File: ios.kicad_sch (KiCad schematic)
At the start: 9 parts, among them SW1 SW_1301_9305_THT, SW2 SW_1301_9305_THT, SW3 SW_1301_9305_THT, SW4 SW_1301_9305_THT

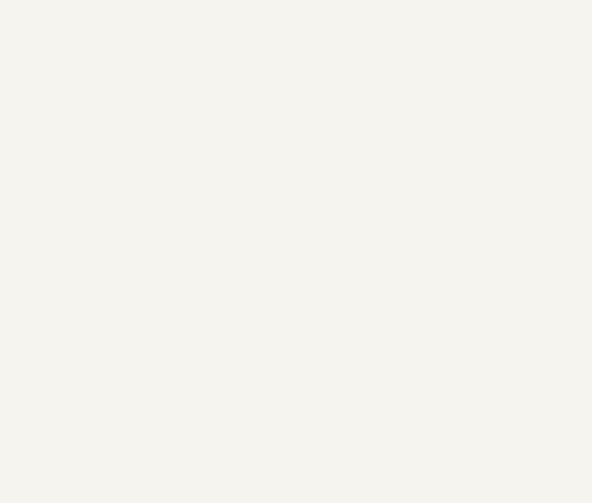
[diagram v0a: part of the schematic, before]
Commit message: [#94684] Add ports to subsheets
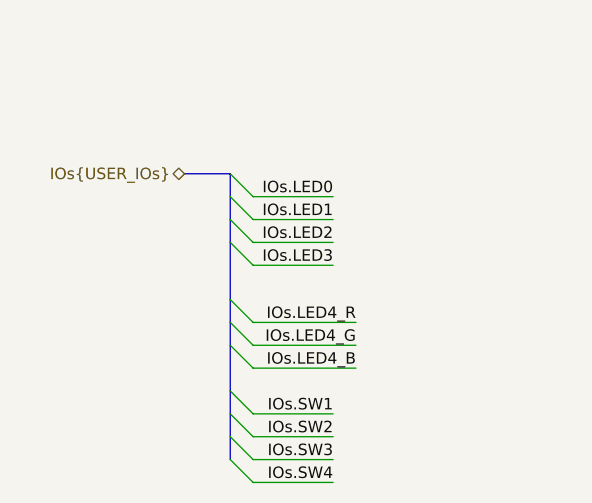
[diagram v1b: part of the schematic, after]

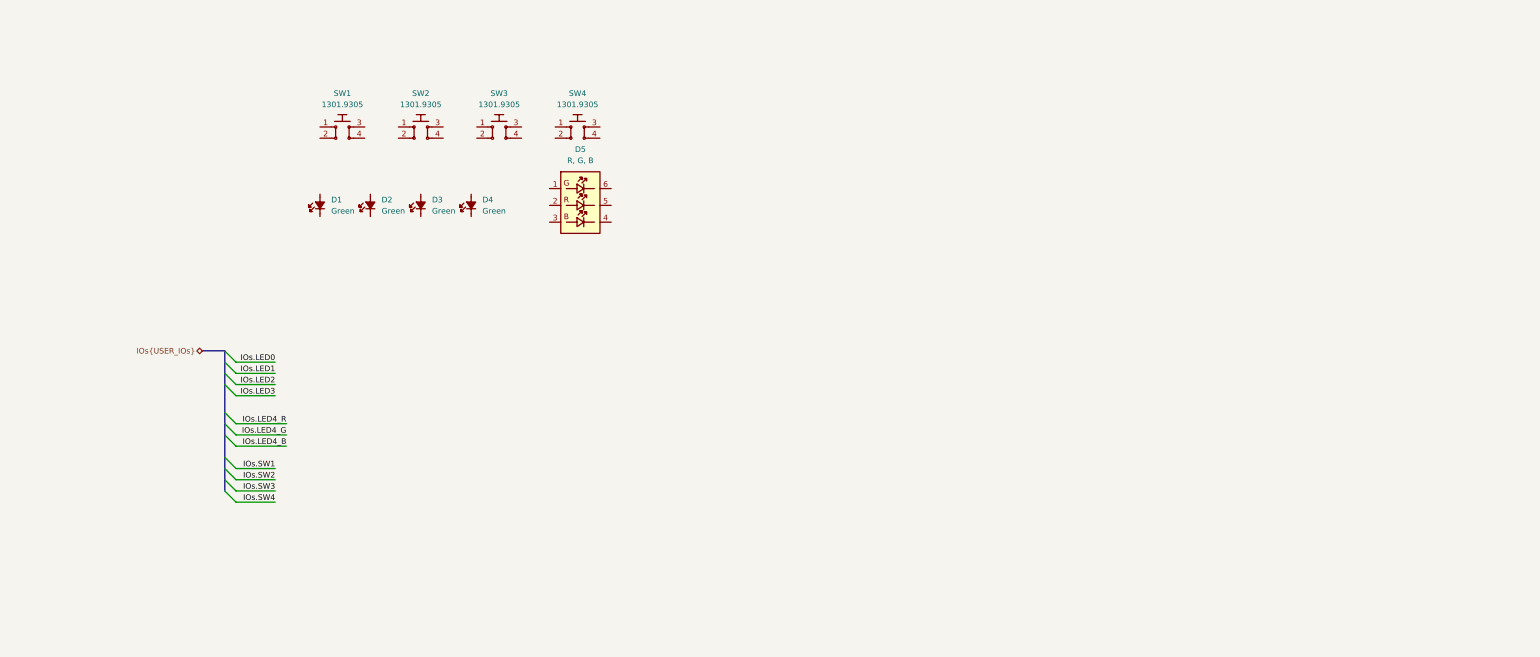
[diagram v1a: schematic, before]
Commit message: [#94883] LED and pushbutton schematic
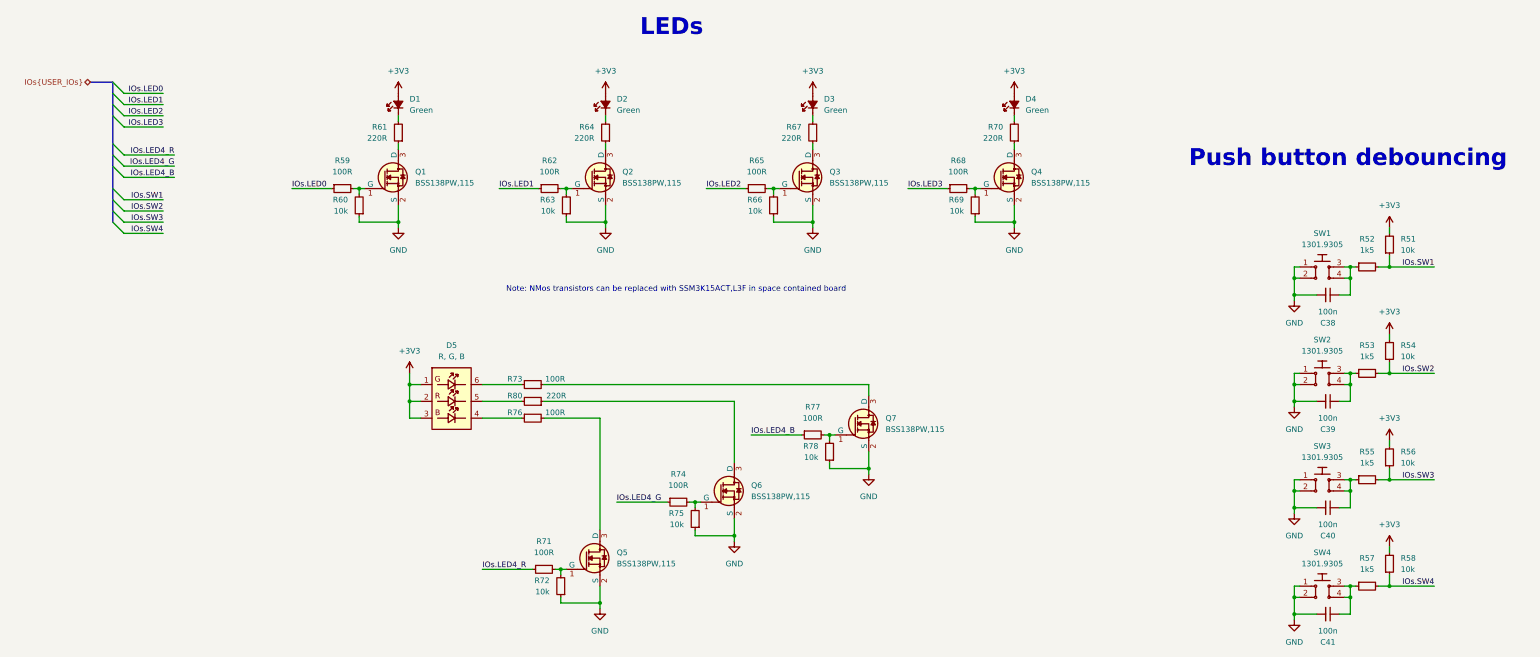
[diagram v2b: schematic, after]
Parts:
- added C38, C39, C40, C41: C_100n_0402, antmicro-footprints:C_0402_1005Metric, symbol antmicroCapacitors0402:C_100n_0402
- added Q1, Q2, Q3, Q4, Q5, Q6, Q7: BSS138PW,115, antmicro-footprints:SC70-3, symbol antmicroTransistorsFETsMOSFETsSingle:BSS138PW,115
- added R51, R54, R56, R58, R60, R63, R66, R69, R72, R75, R78: R_10k_0402, antmicro-footprints:R_0402_1005Metric, symbol antmicroResistors0402:R_10k_0402
- added R52, R53, R55, R57: R_1k5_0402, antmicro-footprints:R_0402_1005Metric, symbol antmicroResistors0402:R_1k5_0402
- added R59, R62, R65, R68, R71, R73, R74, R76, R77: R_100R_0402, antmicro-footprints:R_0402_1005Metric, symbol antmicroResistors0402:R_100R_0402
- added R61, R64, R67, R70, R80: R_220R_0402, antmicro-footprints:R_0402_1005Metric, symbol antmicroResistors0402:R_220R_0402
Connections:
- net IOs.LED0: now also R59.1
- net IOs.LED1: now also R62.1
- net IOs.LED2: now also R65.1
- net IOs.LED3: now also R68.1
- net IOs.LED4_B: now also R77.1
- net IOs.LED4_G: now also R74.1
- net IOs.LED4_R: now also R71.1
- net IOs.SW1: now also R51.1, R52.2
- net IOs.SW2: now also R53.2, R54.1
- net IOs.SW3: now also R55.2, R56.1
- net IOs.SW4: now also R57.2, R58.1
- net GND: now reaches SW4.1
- net GND: now also SW1.1, SW1.2, SW2.1, SW2.2, SW3.1, SW3.2, SW4.2, C38.2, C39.2, C40.2, C41.2, Q1.2 (S), Q2.2 (S), Q3.2 (S), Q4.2 (S), Q5.2 (S), Q6.2 (S), Q7.2 (S), R60.1, R63.1, R66.1, R69.1, R72.1, R75.1, R78.1
- net at SW4.3: now also SW4.4, C41.1, R57.1
- net at D1.1 (C): now also R61.2
- net +3V3: now reaches D1.2 (A)
- net +3V3: now also D2.2 (A), D3.2 (A), D4.2 (A), D5.1 (A_{G}), D5.2 (A_{R}), D5.3 (A_{B}), R51.2, R54.2, R56.2, R58.2
- net at SW3.3: now also SW3.4, C40.1, R55.1
- net at D3.1 (C): now also R67.2
- net at D2.1 (C): now also R64.2
- net at SW2.3: now also SW2.4, C39.1, R53.1
- net at D5.4 (C_{B}): now also R76.1
- net at D5.5 (C_{R}): now also R80.2
- net at D5.6 (C_{G}): now also R73.1
- net at SW1.3: now also SW1.4, C38.1, R52.1
- net at D4.1 (C): now also R70.2
- new net: Q4.1 (G), R68.2, R69.2
- new net: Q5.1 (G), R71.2, R72.2
- new net: Q4.3 (D), R70.1
- new net: Q2.1 (G), R62.2, R63.2
- new net: Q2.3 (D), R64.1
- new net: Q7.1 (G), R77.2, R78.2
- new net: Q6.1 (G), R74.2, R75.2
- new net: Q6.3 (D), R80.1
- new net: Q3.1 (G), R65.2, R66.2
- new net: Q7.3 (D), R73.2
- new net: Q1.1 (G), R59.2, R60.2
- new net: Q5.3 (D), R76.2
- new net: Q3.3 (D), R67.1
- new net: Q1.3 (D), R61.1
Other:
- note added: "LEDs"
- note added: "Note: NMos transistors can be replaced with SSM3K15ACT,L3F in space contained board"
- note added: "Push button debouncing"
- moved on the sheet: D1, D2, D3, D4, D5, SW1

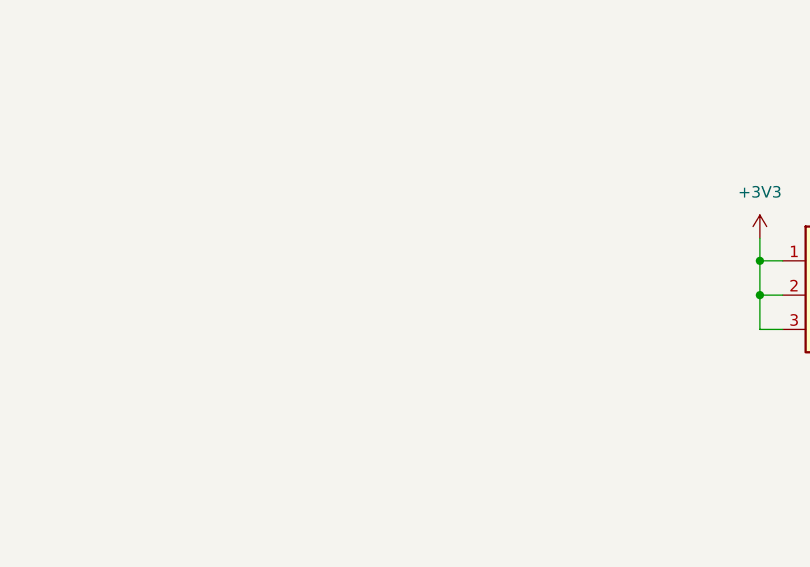
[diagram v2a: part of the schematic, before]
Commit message: [#95036] Add schematic markings
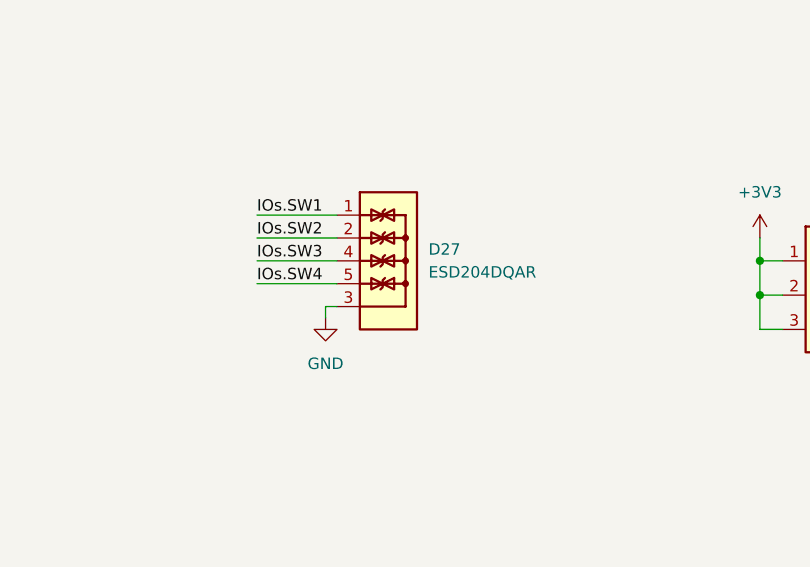
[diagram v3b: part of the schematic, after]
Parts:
- added D27: ESD204DQAR, antmicro-footprints:USON-10_2.5x1mm_P0.5mm, symbol antmicroTVSDiodes:ESD204DQAR
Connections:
- net GND: now also D27.3, D27.8
- net IOs.SW1: now also D27.1, D27.10
- net IOs.SW2: now also D27.2, D27.9
- net IOs.SW3: now also D27.4, D27.7
- net IOs.SW4: now also D27.5, D27.6

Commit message: [#95398] Cleanup
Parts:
- removed SW1, SW2, SW3, SW4: SW_1301_9305_THT, antmicro-footprints:SW_1301_9305_THT, symbol antmicroPushbuttonSwitches:SW_1301_9305_THT
- added C35, C36: C_100n_0402, antmicro-footprints:C_0402_1005Metric, symbol antmicroCapacitors0402:C_100n_0402
- added POT1, POT2: RK09K1110A2S, antmicro-footprints:Trimpot_THT_RK09K1110A2S, symbol antmicroTrimmerPotentiometers:RK09K1110A2S
- added SW1, SW2, SW3, SW4: SW_SKRPABE010, antmicro-footprints:SW_PTS810SJM250SMTRLFS_SMD, symbol antmicroPushbuttonSwitches:SW_SKRPABE010
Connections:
- net +3V3: now also POT1.1, POT2.1
- net GND: now also C35.1, C36.1, POT1.3, POT1.MH, POT2.3, POT2.MH, SW1.1, SW1.2, SW2.1, SW2.2, SW3.1, SW3.2, SW4.1, SW4.2
- net at C39.1, R53.1: now also SW2.3, SW2.4
- net at C38.1, R52.1: now also SW1.3, SW1.4
- net at C41.1, R57.1: now also SW4.3, SW4.4
- net at C40.1, R55.1: now also SW3.3, SW3.4
- new net POT1_Analog: C35.2, POT1.2
- new net POT2_Analog: C36.2, POT2.2
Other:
- moved on the sheet: C38, C39, C40, C41, D1, D2, D27, D3, D4, D5, Q1, Q2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

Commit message: [#95398] Schematic cleanup
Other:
- note added: "Potentiometers"
- note removed: "Note: NMos transistors can be replaced with SSM3K15ACT,L3F in space contained board"
- moved on the sheet: C35, C36, POT1, POT2

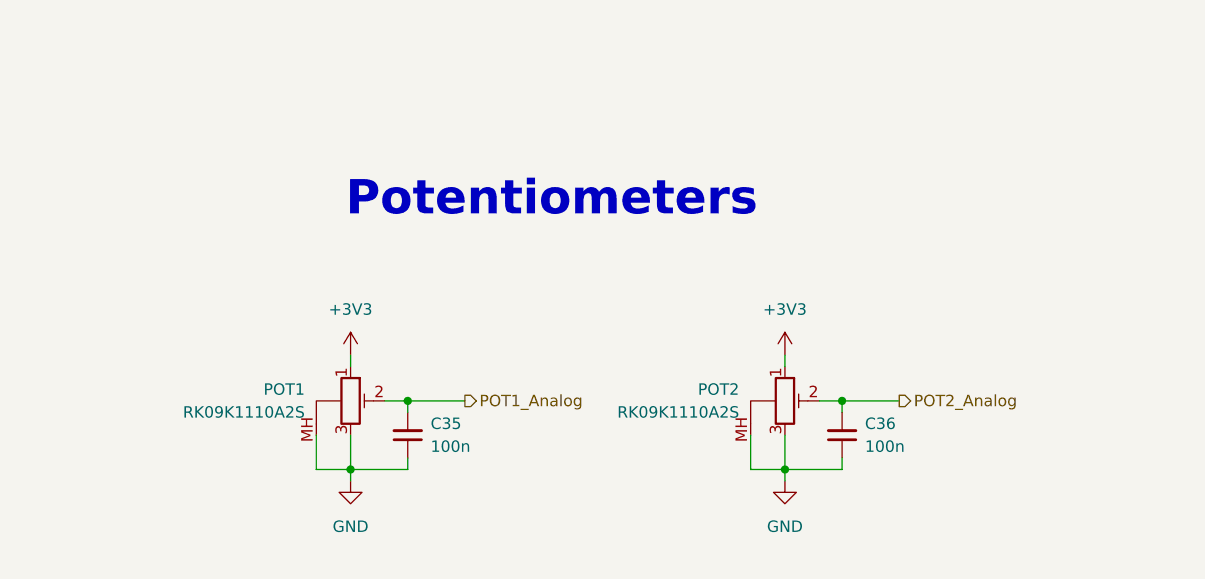
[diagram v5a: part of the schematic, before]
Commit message: [#95398] Mock main components, add BGA MCU
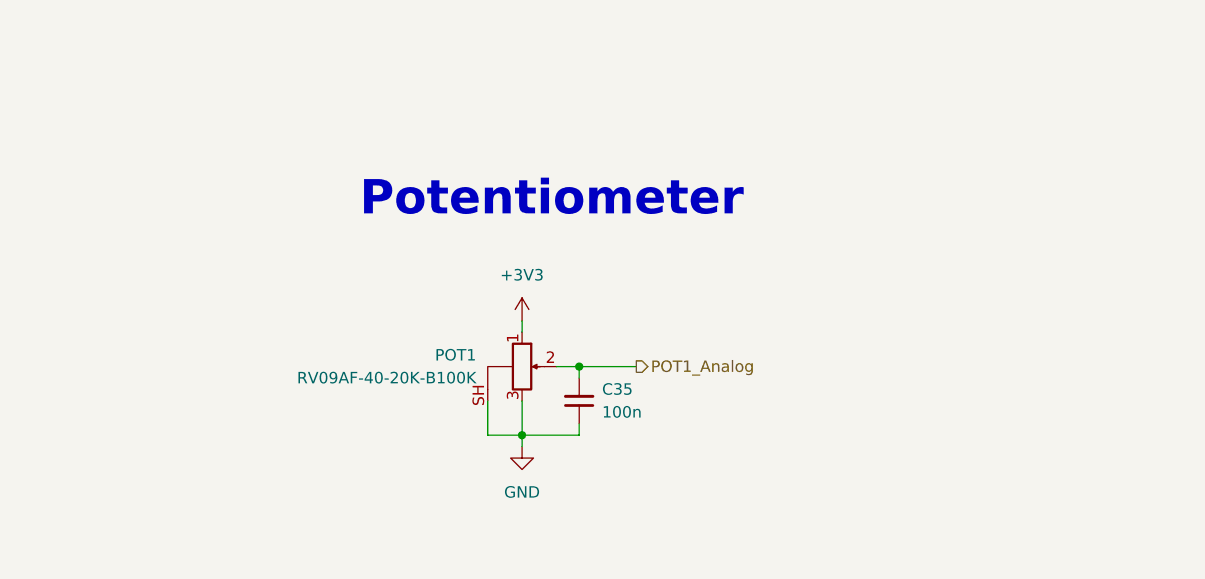
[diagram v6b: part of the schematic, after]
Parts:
- removed C36: C_100n_0402, antmicro-footprints:C_0402_1005Metric, symbol antmicroCapacitors0402:C_100n_0402
- removed POT1, POT2: RK09K1110A2S, antmicro-footprints:Trimpot_THT_RK09K1110A2S, symbol antmicroTrimmerPotentiometers:RK09K1110A2S
- added POT1: POT_100k_RV09AF-40-20K-B100K, antmicro-footprints:POT_RV09AF-40, symbol antmicroRotaryPotentiometersRheostats:POT_100k_RV09AF-40-20K-B100K
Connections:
- net +3V3: now also POT1.1
- net GND: now also POT1.3, POT1.SH
- net POT1_Analog: now also POT1.2
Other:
- note added: "Potentiometer"
- note removed: "Potentiometers"
- moved on the sheet: C35

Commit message: [#95398] Add markings for ETH strap resistors
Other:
- title: renode-reference-platform -> STM32H7 Renode Reference Platform
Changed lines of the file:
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@@
 	(paper "A3")
 	(title_block
-		(title "renode-reference-platform")
+		(title "STM32H7 Renode Reference Platform")
 		(date "07.04.2026")
 		(rev "1.0.0")

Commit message: [#95451] Finalizing final placement
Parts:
- removed Q1, Q2, Q3, Q5, Q6, Q7: BSS138PW,115, antmicro-footprints:SC70-3, symbol antmicroTransistorsFETsMOSFETsSingle:BSS138PW,115
- removed R59, R62, R65, R71, R74, R77: R_100R_0402, antmicro-footprints:R_0402_1005Metric, symbol antmicroResistors0402:R_100R_0402
- removed R60, R63, R66, R72, R75, R78: R_10k_0402, antmicro-footprints:R_0402_1005Metric, symbol antmicroResistors0402:R_10k_0402
- added C116: C_100n_0402, antmicro-footprints:C_0402_1005Metric, symbol antmicroCapacitors0402:C_100n_0402
- added U25: 74LVC06ABQ, antmicro-footprints:DHVQFN-14-1EP_2.5x3mm, symbol antmicroLogicBuffersDriversReceiversTransceivers:74LVC06ABQ
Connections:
- net +3V3: now also C116.2, U25.14 (V_{CC})
- net GND: now also C116.1, U25.15 (GND), U25.7 (GND)
- net IOs.LED0: now also U25.1 (1A)
- net IOs.LED1: now also U25.3 (2A)
- net IOs.LED2: now also U25.5 (3A)
- net IOs.LED4_B: now also U25.13 (6A)
- net IOs.LED4_G: now also U25.9 (4A)
- net IOs.LED4_R: now also U25.11 (5A)
- net at R64.1: now also D2.1 (C)
- net at R80.1: now also U25.10 (5Y)
- net at R73.2: now also U25.8 (4Y)
- net at R67.2: now also U25.6 (3Y); no longer D3.1 (C)
- net at R64.2: now also U25.4 (2Y); no longer D2.1 (C)
- net at R76.2: now also U25.12 (6Y)
- net at R67.1: now also D3.1 (C)
- net at R61.1: now also U25.2 (1Y)
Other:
- moved on the sheet: C38, C39, C40, C41, D1, D2, D27, D3, D4, D5, Q4, R51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
